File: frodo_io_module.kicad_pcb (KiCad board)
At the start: 4 copper layers, 58 x 58 mm, 198 parts, among them J1 Molex MicroFit 2x3, J10 Molex MicroFit 2x2, J11 Molex MicroFit 2x2, J12 JST-GH 4Pin, J13 JST-GH 4Pin, J2 Molex MicroFit 2x3, J3 SWD, J4 JST-GH 4Pin, J5 JST-GH 4Pin, J6 JST-GH 4Pin, J7 JST-GH 4Pin, J8 Molex MicroFit 2x2, J9 Molex MicroFit 2x2, Q1 NMOS, Q10 PMOS, Q11 PMOS, Q12 PMOS, Q13 PMOS, Q14 PMOS, Q15 PMOS, Q16 PMOS, Q17 NMOS, Q18 NMOS, Q2 NMOS, Q3 NMOS, Q4 NMOS, Q5 NMOS, Q6 NMOS, Q7 NMOS, Q8 NMOS, Q9 PMOS, SW1 SW_DIP_x06, U1 AZ1117H-ADJ, U10 STM32F103RCTx, U2 INA213, U3 AZ1117-3.3, U4 W25Q128JVP, U5 MCP2562-E-SN, U6 L7805, U7 L7805, U8 MCP4017-xxxxLT, U9 LM3488MM, Y1 8MHz 12pF

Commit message: add descriptors on silkscreen, add part numbers
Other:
- board text added: "5V"
- board text added: "BAT"
- board text added: "BST"
- board text added: "BUS A"
- board text added: "BUS B"
- board text added: "CHR"
- board text added: "COM0"
- board text added: "COM1"
- board text added: "COM2"
- board text added: "COM3"
- board text added: "COM4"
- board text added: "COM5"
- board text added: "OUT0"
- board text added: "OUT1"
- board text added: "OUT2"
- board text added: "OUT3"

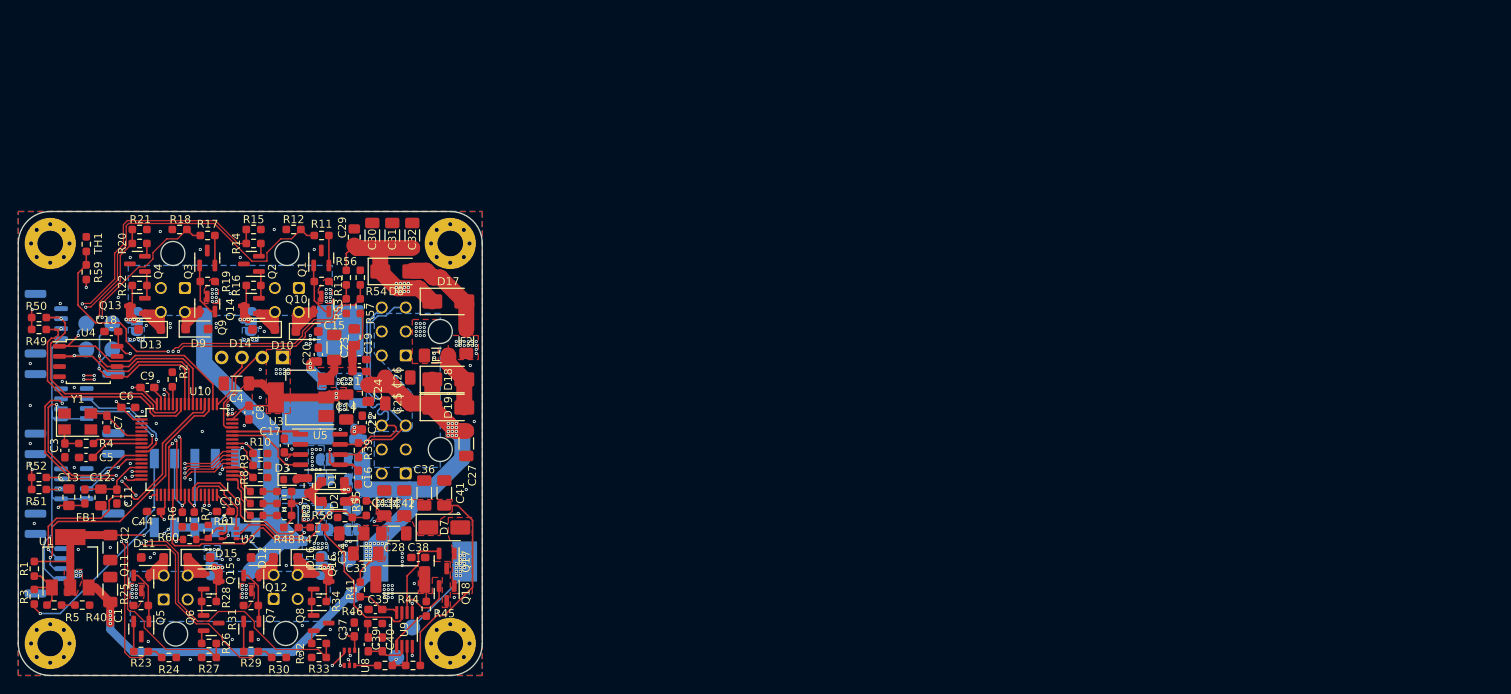
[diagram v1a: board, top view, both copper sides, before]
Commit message: updated scematic to new requirements
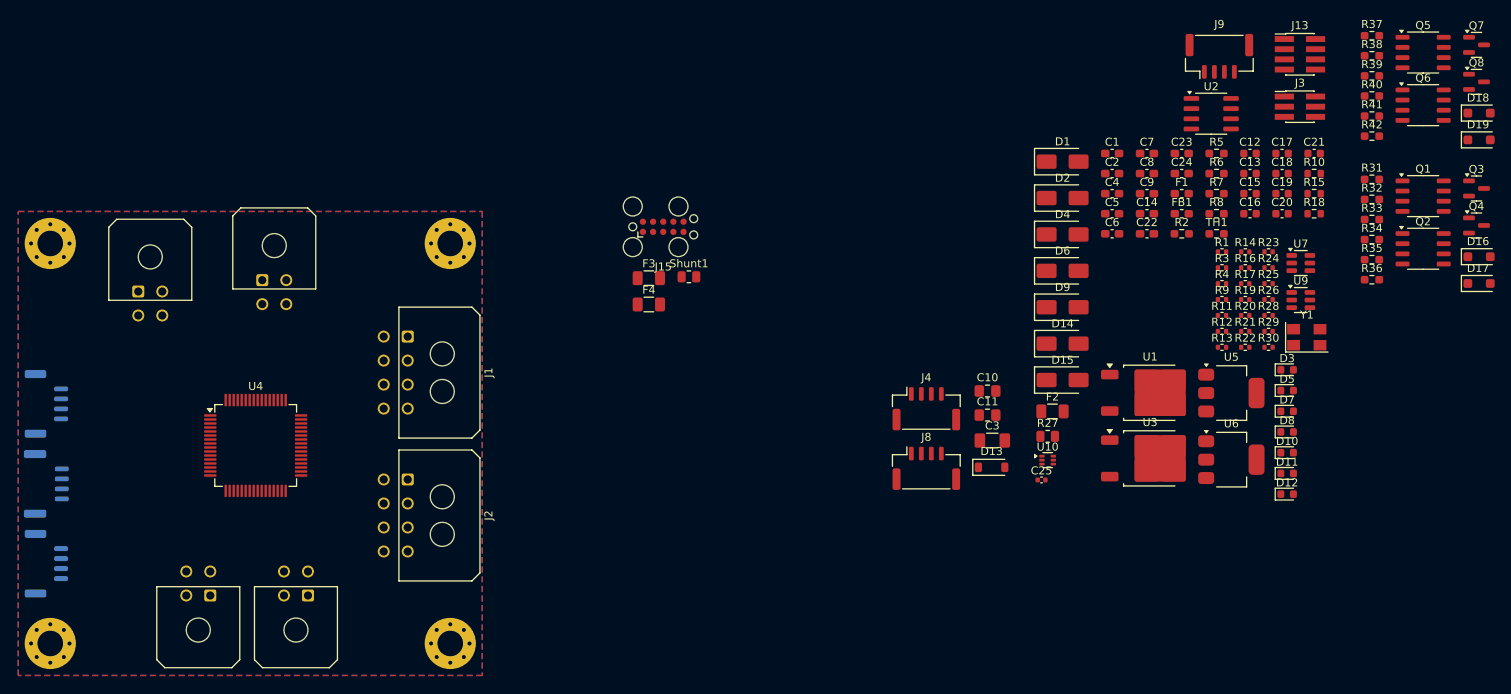
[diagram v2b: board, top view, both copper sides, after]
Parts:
- removed C26, C27, C28, C30, C31, C32, C33, C34: 22u, Capacitor_SMD:C_1206_3216Metric_Pad1.33x1.80mm_HandSolder
- removed C29: 1u, Capacitor_SMD:C_0805_2012Metric_Pad1.18x1.45mm_HandSolder
- removed C35, C37, C39, C44: 100n, Capacitor_SMD:C_0603_1608Metric_Pad1.08x0.95mm_HandSolder
- removed C36, C41, C42, C43: 10u, Capacitor_SMD:C_1206_3216Metric_Pad1.33x1.80mm_HandSolder
- removed C38: 10p, Capacitor_SMD:C_0603_1608Metric_Pad1.08x0.95mm_HandSolder
- removed C40: 3.3n, Capacitor_SMD:C_0603_1608Metric_Pad1.08x0.95mm_HandSolder
- removed G***: LOGO, frodo_io_module:rapid_logo
- removed JP1, JP2: +VSW_Sel, Jumper:SolderJumper-2_P1.3mm_Open_RoundedPad1.0x1.5mm
- removed JP10, JP11, JP12, JP9: servo_ss, Jumper:SolderJumper-3_P1.3mm_Open_RoundedPad1.0x1.5mm
- removed JP3, JP4: VDC_Sel, Jumper:SolderJumper-2_P1.3mm_Open_RoundedPad1.0x1.5mm
- removed JP5, JP6: Vext_Sel, Jumper:SolderJumper-2_P1.3mm_Open_RoundedPad1.0x1.5mm
- removed JP7, JP8: +5V_Sel, Jumper:SolderJumper-2_P1.3mm_Open_RoundedPad1.0x1.5mm
- removed L1: 15u, Inductor_SMD:L_Bourns_SRP1245A
- removed Q10, Q11, Q12, Q13, Q14, Q15, Q16, Q9: PMOS, Package_TO_SOT_SMD:SOT-23
- removed Q17, Q18: NMOS, Package_TO_SOT_SMD:SOT-23
- removed R43: 33k, Resistor_SMD:R_0603_1608Metric_Pad0.98x0.95mm_HandSolder
- removed R44: 10m, Resistor_SMD:R_2512_6332Metric_Pad1.40x3.35mm_HandSolder
- removed R45: 100, Resistor_SMD:R_0603_1608Metric_Pad0.98x0.95mm_HandSolder
- removed R46, R48: 1.5k, Resistor_SMD:R_0603_1608Metric_Pad0.98x0.95mm_HandSolder
- removed R47: 47k, Resistor_SMD:R_0603_1608Metric_Pad0.98x0.95mm_HandSolder
- removed R49, R50, R51, R52, R53: 4.7k, Resistor_SMD:R_0603_1608Metric_Pad0.98x0.95mm_HandSolder
- removed R54: 15k, Resistor_SMD:R_0603_1608Metric_Pad0.98x0.95mm_HandSolder
- removed R55: 22k, Resistor_SMD:R_0603_1608Metric_Pad0.98x0.95mm_HandSolder
- removed R56, R57, R58: 2.2k, Resistor_SMD:R_0603_1608Metric_Pad0.98x0.95mm_HandSolder
- removed R59: 10k, Resistor_SMD:R_0603_1608Metric_Pad0.98x0.95mm_HandSolder
- removed R60, R61: 10k, Resistor_SMD:R_0603_1608Metric
- removed R62: 5m, Resistor_SMD:R_2512_6332Metric
- removed SW1: SW_DIP_x06, Button_Switch_SMD:SW_DIP_SPSTx06_Slide_9.78x17.42mm_W8.61mm_P2.54mm
- removed TP1, TP10, TP2, TP3, TP4, TP7, TP8, TP9: TestPoint, TestPoint:TestPoint_Pad_D2.0mm
- removed U8: MCP4017-xxxxLT, Package_TO_SOT_SMD:SOT-363_SC-70-6
- added F3: 10A, Fuse:Fuse_1206_3216Metric, F.Cu at (178.8, 108.3)
- added F4: 10A, Fuse:Fuse_1206_3216Metric, F.Cu at (178.8, 111.6)
- added J14: ~, stigma:Molex_Micro-Fit_3.0_43045-0400_2x02_P3.00mm_Horizontal, F.Cu at (115.0, 110.0)
- added J15: TC2050, Connector:Tag-Connect_TC2050-IDC-FP_2x05_P1.27mm_Vertical, F.Cu at (180.6, 101.9)
- added Shunt1: 250mR 1%, Resistor_SMD:R_0805_2012Metric, F.Cu at (183.8, 108.2)
- C1, C4: value 10u -> 100n; footprint Capacitor_SMD:C_1206_3216Metric_Pad1.33x1.80mm_HandSolder -> Capacitor_SMD:C_0603_1608Metric_Pad1.08x0.95mm_HandSolder
- C10: value 100n -> 1u; footprint Capacitor_SMD:C_0603_1608Metric_Pad1.08x0.95mm_HandSolder -> Capacitor_SMD:C_0805_2012Metric_Pad1.18x1.45mm_HandSolder
- C11: value 22n -> 1u; footprint Capacitor_SMD:C_0603_1608Metric_Pad1.08x0.95mm_HandSolder -> Capacitor_SMD:C_0805_2012Metric_Pad1.18x1.45mm_HandSolder
- C12: value 1u -> 330n; footprint Capacitor_SMD:C_0805_2012Metric_Pad1.18x1.45mm_HandSolder -> Capacitor_SMD:C_0603_1608Metric
- C13: value 1u -> 100n; footprint Capacitor_SMD:C_0805_2012Metric_Pad1.18x1.45mm_HandSolder -> Capacitor_SMD:C_0603_1608Metric
- C14, C2: value 22u -> 100n; footprint Capacitor_SMD:C_1206_3216Metric_Pad1.33x1.80mm_HandSolder -> Capacitor_SMD:C_0603_1608Metric_Pad1.08x0.95mm_HandSolder
- C15: value 10u -> 330n; footprint Capacitor_SMD:C_1206_3216Metric_Pad1.33x1.80mm_HandSolder -> Capacitor_SMD:C_0603_1608Metric
- C16: footprint Capacitor_SMD:C_0603_1608Metric_Pad1.08x0.95mm_HandSolder -> Capacitor_SMD:C_0603_1608Metric
- C17, C20: value 100n -> 10u; footprint Capacitor_SMD:C_0603_1608Metric_Pad1.08x0.95mm_HandSolder -> Capacitor_SMD:C_0603_1608Metric
- C18: value 100n -> 22u; footprint Capacitor_SMD:C_0603_1608Metric_Pad1.08x0.95mm_HandSolder -> Capacitor_SMD:C_0603_1608Metric
- C19: value 330n -> 100n; footprint Capacitor_SMD:C_0603_1608Metric_Pad1.08x0.95mm_HandSolder -> Capacitor_SMD:C_0603_1608Metric
- C21: value 330n -> 22u; footprint Capacitor_SMD:C_0603_1608Metric_Pad1.08x0.95mm_HandSolder -> Capacitor_SMD:C_0603_1608Metric
- C22: value 100n -> 10p
- C23: value 1u -> 10p; footprint Capacitor_SMD:C_0805_2012Metric_Pad1.18x1.45mm_HandSolder -> Capacitor_SMD:C_0603_1608Metric_Pad1.08x0.95mm_HandSolder
- C24: value 1u -> 100n; footprint Capacitor_SMD:C_0805_2012Metric_Pad1.18x1.45mm_HandSolder -> Capacitor_SMD:C_0603_1608Metric_Pad1.08x0.95mm_HandSolder
- C25: value 22u -> 100n; footprint Capacitor_SMD:C_1206_3216Metric_Pad1.33x1.80mm_HandSolder -> Capacitor_SMD:C_0402_1005Metric
- C3: value 10p -> 10u; footprint Capacitor_SMD:C_0603_1608Metric_Pad1.08x0.95mm_HandSolder -> Capacitor_SMD:C_1206_3216Metric_Pad1.33x1.80mm_HandSolder
- C7: value 10p -> 100n
- C9: value 100n -> 22n
- D1: value D_Schottky -> D; footprint Diode_SMD:D_SOD-123F -> Diode_SMD:D_SMA
- D10, D12: value D -> LED; footprint Diode_SMD:D_SOD-123F -> LED_SMD:LED_0603_1608Metric
- D11: value D -> red; footprint Diode_SMD:D_SOD-123F -> LED_SMD:LED_0603_1608Metric
- D13: value D -> NRVB130T1G; footprint Diode_SMD:D_SOD-123F -> Diode_SMD:D_SOD-123
- D14, D15: footprint Diode_SMD:D_SOD-123F -> Diode_SMD:D_SMA
- D17, D18, D19: value D_Schottky -> D; footprint Diode_SMD:D_SMA -> Diode_SMD:D_SOD-123F
- D2: value D_Schottky -> SS34; footprint Diode_SMD:D_SOD-123F -> Diode_SMD:D_SMA
- D3, D5: value LED -> red
- D4, D6: value LED -> SS34; footprint LED_SMD:LED_0603_1608Metric -> Diode_SMD:D_SMA
- D7: value D_Schottky -> red; footprint Diode_SMD:D_SMA -> LED_SMD:LED_0603_1608Metric
- D8: value D_Schottky -> LED; footprint Diode_SMD:D_SMA -> LED_SMD:LED_0603_1608Metric
- D9: value D -> SS34; footprint Diode_SMD:D_SOD-123F -> Diode_SMD:D_SMA
- F1: value 10A -> 3A; footprint Fuse:Fuse_1206_3216Metric_Pad1.42x1.75mm_HandSolder -> Fuse:Fuse_0603_1608Metric_Pad1.05x0.95mm_HandSolder
- F2: footprint Fuse:Fuse_1206_3216Metric_Pad1.42x1.75mm_HandSolder -> Fuse:Fuse_1206_3216Metric
- J1, J2: value Molex MicroFit 2x3 -> Conn_02x04_Top_Bottom; footprint Connector_Molex:Molex_Micro-Fit_3.0_43045-0600_2x03_P3.00mm_Horizontal -> Connector_Molex:Molex_Micro-Fit_3.0_43045-0800_2x04_P3.00mm_Horizontal; moved to F.Cu
- J10, J11: value Molex MicroFit 2x2 -> ~; footprint Connector_Molex:Molex_Micro-Fit_3.0_43045-0400_2x02_P3.00mm_Horizontal -> stigma:Molex_Micro-Fit_3.0_43045-0400_2x02_P3.00mm_Horizontal; moved to F.Cu
- J12: value JST-GH 4Pin -> ~; footprint Connector_JST:JST_GH_BM04B-GHS-TBT_1x04-1MP_P1.25mm_Vertical -> stigma:Molex_Micro-Fit_3.0_43045-0400_2x02_P3.00mm_Horizontal; moved to F.Cu
- J13: value JST-GH 4Pin -> Conn_02x05_Counter_Clockwise; footprint Connector_JST:JST_GH_BM04B-GHS-TBT_1x04-1MP_P1.25mm_Vertical -> Connector_PinHeader_1.27mm:PinHeader_2x04_P1.27mm_Vertical_SMD; moved to F.Cu
- J3: value SWD -> Conn_02x03_Counter_Clockwise; footprint Connector_PinHeader_2.54mm:PinHeader_1x04_P2.54mm_Vertical -> Connector_PinHeader_1.27mm:PinHeader_2x03_P1.27mm_Vertical_SMD; moved to F.Cu
- J4: moved to F.Cu
- J6: footprint Connector_JST:JST_GH_SM04B-GHS-TB_1x04-1MP_P1.25mm_Horizontal -> Connector_JST:JST_GH_BM04B-GHS-TBT_1x04-1MP_P1.25mm_Vertical
- J8: value Molex MicroFit 2x2 -> JST-GH 4Pin; footprint Connector_Molex:Molex_Micro-Fit_3.0_43045-0400_2x02_P3.00mm_Horizontal -> Connector_JST:JST_GH_SM04B-GHS-TB_1x04-1MP_P1.25mm_Horizontal; moved to F.Cu
- J9: value Molex MicroFit 2x2 -> JST-GH 4Pin; footprint Connector_Molex:Molex_Micro-Fit_3.0_43045-0400_2x02_P3.00mm_Horizontal -> Connector_JST:JST_GH_BM04B-GHS-TBT_1x04-1MP_P1.25mm_Vertical; moved to F.Cu
- Q1, Q2, Q5, Q6: value NMOS -> AOSP21321; footprint Package_TO_SOT_SMD:SOT-23 -> Package_SO:SO-8_3.9x4.9mm_P1.27mm
- R1: value 680 -> 220; footprint Resistor_SMD:R_0603_1608Metric_Pad0.98x0.95mm_HandSolder -> Resistor_SMD:R_0402_1005Metric
- R10: value 10K -> 220; footprint Resistor_SMD:R_0603_1608Metric_Pad0.98x0.95mm_HandSolder -> Resistor_SMD:R_0603_1608Metric
- R11, R17: value 330 -> 310R; footprint Resistor_SMD:R_0603_1608Metric_Pad0.98x0.95mm_HandSolder -> Resistor_SMD:R_0402_1005Metric
- R12: value 10k -> 1k; footprint Resistor_SMD:R_0603_1608Metric_Pad0.98x0.95mm_HandSolder -> Resistor_SMD:R_0402_1005Metric
- R13, R16, R19, R4: value 1k -> 220; footprint Resistor_SMD:R_0603_1608Metric_Pad0.98x0.95mm_HandSolder -> Resistor_SMD:R_0402_1005Metric
- R14: value 330 -> 150R; footprint Resistor_SMD:R_0603_1608Metric_Pad0.98x0.95mm_HandSolder -> Resistor_SMD:R_0402_1005Metric
- R15: value 10k -> 220; footprint Resistor_SMD:R_0603_1608Metric_Pad0.98x0.95mm_HandSolder -> Resistor_SMD:R_0603_1608Metric
- R18: value 10k -> 60R; footprint Resistor_SMD:R_0603_1608Metric_Pad0.98x0.95mm_HandSolder -> Resistor_SMD:R_0603_1608Metric
- R2: value 10k -> 120, DNP
- R20: value 330 -> 22; footprint Resistor_SMD:R_0603_1608Metric_Pad0.98x0.95mm_HandSolder -> Resistor_SMD:R_0402_1005Metric
- R21: value 10k -> 22; footprint Resistor_SMD:R_0603_1608Metric_Pad0.98x0.95mm_HandSolder -> Resistor_SMD:R_0402_1005Metric
- R22: value 1k -> 22; footprint Resistor_SMD:R_0603_1608Metric_Pad0.98x0.95mm_HandSolder -> Resistor_SMD:R_0402_1005Metric
- R23, R26: value 330 -> 5k; footprint Resistor_SMD:R_0603_1608Metric_Pad0.98x0.95mm_HandSolder -> Resistor_SMD:R_0402_1005Metric
- R24: value 10k -> 5k; footprint Resistor_SMD:R_0603_1608Metric_Pad0.98x0.95mm_HandSolder -> Resistor_SMD:R_0402_1005Metric
- R25: value 1k -> 5k; footprint Resistor_SMD:R_0603_1608Metric_Pad0.98x0.95mm_HandSolder -> Resistor_SMD:R_0402_1005Metric
- R27: value 10k -> 10m; footprint Resistor_SMD:R_0603_1608Metric_Pad0.98x0.95mm_HandSolder -> Resistor_SMD:R_0805_2012Metric
- R28: value 1k -> 15k; footprint Resistor_SMD:R_0603_1608Metric_Pad0.98x0.95mm_HandSolder -> Resistor_SMD:R_0402_1005Metric
- R29: value 330 -> 15k; footprint Resistor_SMD:R_0603_1608Metric_Pad0.98x0.95mm_HandSolder -> Resistor_SMD:R_0402_1005Metric
- R3: value 820 -> 10k; footprint Resistor_SMD:R_0603_1608Metric_Pad0.98x0.95mm_HandSolder -> Resistor_SMD:R_0402_1005Metric
- R30: value 10k -> 15k; footprint Resistor_SMD:R_0603_1608Metric_Pad0.98x0.95mm_HandSolder -> Resistor_SMD:R_0402_1005Metric
- R32: value 330 -> 1k
- R33: value 10k -> 330
- R34: value 1k -> 330
- R35, R36: value 220 -> 10k
- R37: value 680 -> 1k
- R38: value 220 -> 1k
- R39: value 120, DNP -> 330
- R40: value 100 -> 330
- R41: value 22 -> 10k
- R42: value 1.5k -> 10k
- R5: value 1k -> 4.7k
- R6, R7, R8: value 10K -> 4.7k
- R9: value 10K -> 150R; footprint Resistor_SMD:R_0603_1608Metric_Pad0.98x0.95mm_HandSolder -> Resistor_SMD:R_0402_1005Metric
- U1: value AZ1117H-ADJ -> L7805; footprint Package_TO_SOT_SMD:SOT-223-3_TabPin2 -> Package_TO_SOT_SMD:TO-252-2
- U10: value STM32F103RCTx -> TPD4E1U06; footprint Package_QFP:LQFP-64_10x10mm_P0.5mm -> Package_TO_SOT_SMD:SOT-563
- U2: value INA213 -> MCP2562-E-SN; footprint Package_TO_SOT_SMD:SOT-363_SC-70-6 -> Package_SO:SOIC-8_3.9x4.9mm_P1.27mm
- U3: value AZ1117-3.3 -> L7805; footprint Package_TO_SOT_SMD:SOT-223-3_TabPin2 -> Package_TO_SOT_SMD:TO-252-2
- U4: value W25Q128JVP -> STM32F103RCTx; footprint Package_SO:SOIC-8_5.275x5.275mm_P1.27mm -> Package_QFP:LQFP-64_10x10mm_P0.5mm
- U5: value MCP2562-E-SN -> AZ1117H-ADJ; footprint Package_SO:SOIC-8_3.9x4.9mm_P1.27mm -> Package_TO_SOT_SMD:SOT-223-3_TabPin2
- U6: value L7805 -> AZ1117H-ADJ; footprint Package_TO_SOT_SMD:TO-252-2 -> Package_TO_SOT_SMD:SOT-223-3_TabPin2; moved to F.Cu
- U7: value L7805 -> INA181; footprint Package_TO_SOT_SMD:TO-252-2 -> Package_TO_SOT_SMD:SOT-23-6; moved to F.Cu
- U9: value LM3488MM -> INA181A2IDBVT; footprint Package_SO:MSOP-8_3x3mm_P0.65mm -> Package_TO_SOT_SMD:SOT-23-6
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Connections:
- C1 pad 1: +VSW_fused -> GND
- C1 pad 2: GND -> +3.3V
- C10 pad 1: +3.3V -> +3.3VA
- C11 pad 1: +3.3VA -> +3.3V
- C12 pad 1: +3.3VA -> GND
- C12 pad 2: GND -> main_voltage
- C13 pad 1: +3.3V -> GND
- C13 pad 2: GND -> Net-(D2-A)
- C14 pad 1: +3.3V -> NRST
- C15 pad 1: +VSW_fused -> GND
- C15 pad 2: GND -> main_voltage
- C16 pad 2: +3.3V -> Net-(D4-A)
- C18 pad 2: +3.3V -> Net-(D6-A)
- C19 pad 1: +VSW_fused -> +3.3V
- C2 pad 1: VSwitch -> GND
- C2 pad 2: GND -> +5V
- C20 pad 1: Net-(D1-A) -> GND
- C20 pad 2: GND -> +5V
- C21 pad 1: +VSW_fused -> GND
- C21 pad 2: GND -> Net-(D9-A)
- C22 pad 1: Net-(D2-A) -> Net-(C22-Pad1)
- C23 pad 1: +VSW_fused -> HSE_IN
- C24 pad 1: +VSW_fused -> GND
- C24 pad 2: GND -> +3.3V
- C25 pad 1: +VSW_fused -> GND
- C25 pad 2: GND -> +5V
- C3 pad 1: Net-(C3-Pad1) -> +3.3V
- C5 pad 1: /NRST -> +3.3V
- C7 pad 1: HSE_IN -> +3.3V
- C9 pad 1: +3.3V -> +3.3VA
- D1 pad 1: +5V -> Net-(D1-K)
- D10 pad 1: Net-(D10-K) -> STAT_LED1
- D10 pad 2: GND -> Net-(D10-A)
- D11 pad 1: Net-(D11-K) -> GND
- D11 pad 2: GND -> Net-(D11-A)
- D12 pad 1: Net-(D12-K) -> STAT_LED2
- D12 pad 2: GND -> Net-(D12-A)
- D13 pad 1: Net-(D13-K) -> /Digital Output/OUT1
- D13 pad 2: GND -> Net-(D13-A)
- D14 pad 1: Net-(D14-K) -> v_main_pre_sense
- D14 pad 2: GND -> high_current2
- D15 pad 1: Net-(D15-K) -> v_main_pre_sense
- D15 pad 2: GND -> high_current
- D16 pad 1: Net-(D16-K) -> /Digital Output/OUT1
- D17 pad 1: VDC_fused -> /Digital Output/OUT2
- D17 pad 2: Net-(D17-A) -> GND
- D18 pad 1: +VSW_fused -> /Digital Output1/OUT1
- D18 pad 2: Net-(D18-A) -> GND
- D19 pad 1: +VSW_fused -> /Digital Output1/OUT2
- D19 pad 2: Net-(D18-A) -> GND
- D4 pad 1: STAT_LED0 -> +5V
- D5 pad 1: STAT_LED1 -> GND
- D6 pad 1: STAT_LED2 -> +3.3V
- D7 pad 1: Vboost -> GND
- D7 pad 2: Vboost_FET_D -> Net-(D7-A)
- D8 pad 1: VDC_fused -> STAT_LED0
- D8 pad 2: Net-(D17-A) -> Net-(D8-A)
- D9 pad 1: Net-(D9-K) -> +3.3V
- D9 pad 2: GND -> Net-(D9-A)
- F1 pad 1: +VSW -> Net-(D1-K)
- F1 pad 2: Net-(D18-A) -> v_main_pre_sense
- F2 pad 1: VDC -> /Digital Output/VD
- F2 pad 2: Net-(D17-A) -> high_current
- J1 pad 3: CAN- -> CAN_1_L
- J1 pad 4: VDC -> CAN_2_L
- J1 pad 5: +VSW -> charging_voltage
- J1 pad 6: CAN+ -> Net-(D1-A)
- J10 pad 3: Net-(D11-K) -> high_current
- J10 pad 4: Net-(D15-K) -> high_current
- J11 pad 3: Net-(D12-K) -> /Digital Output/OUT2
- J11 pad 4: Net-(D16-K) -> /Digital Output/OUT1
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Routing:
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- removed copper zone on F.Cu, net +3.3V
- removed copper zone on In2.Cu, net +3.3V
- removed copper zone on B.Cu, net +5V
- removed copper zone on F.Cu, net +5V
- removed copper zone on B.Cu, net +VSW
- removed copper zone on F.Cu, net +VSW
- removed copper zone on B.Cu, net +VSW_fused
- removed copper zone on F.Cu, net +VSW_fused
- removed copper zone on F.Cu, net VDC
- removed copper zone on In2.Cu, net VDC
- removed copper zone on B.Cu, net VDC_fused
- removed copper zone on In2.Cu, net VDC_fused
- removed copper zone on B.Cu, net VSwitch
- removed copper zone on F.Cu, net VSwitch
- removed copper zone on B.Cu, net Vboost
- removed copper zone on F.Cu, net Vboost
- removed copper zone on F.Cu, net Vboost_FET_D
- removed copper zone on F.Cu, net Vboost_FET_S
- removed copper zone on B.Cu, net Vdrive
- removed copper zone on F.Cu, net Vdrive
- removed copper zone on B.Cu, net Vdrive_pre_I_sense
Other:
- board outline removed
- board text added: "RAPID IO Board"
- board text added: "rev 2"
- board text removed: "5V"
- board text removed: "BAT"
- board text removed: "BST"
- board text removed: "BUS A"
- board text removed: "BUS B"
- board text removed: "CHR"
- board text removed: "FRoDO IO Board"
- board text removed: "OUT0"
- board text removed: "OUT1"
- board text removed: "OUT2"
- board text removed: "OUT3"
- board text removed: "rev 1"

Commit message: some more changes to the io board
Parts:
- removed D17, D18, D19: D, Diode_SMD:D_SOD-123F
- removed J13: Conn_02x05_Counter_Clockwise, Connector_PinHeader_1.27mm:PinHeader_2x04_P1.27mm_Vertical_SMD
- removed R1: 220, Resistor_SMD:R_0402_1005Metric
- removed R3: 10k, Resistor_SMD:R_0402_1005Metric
- added C26: 100n, Capacitor_SMD:C_0402_1005Metric, F.Cu at (126.0, 29.2)
- added C27: 100n, Capacitor_SMD:C_0402_1005Metric, F.Cu at (-215.1, 156.2)
- added C28: 100n, Capacitor_SMD:C_0402_1005Metric, F.Cu at (-195.0, 164.6)
- added C29: 100n, Capacitor_SMD:C_0402_1005Metric, F.Cu at (57.1, 30.8)
- added C30: 100n, Capacitor_SMD:C_0402_1005Metric, F.Cu at (57.1, 32.8)
- added D21: D, Diode_SMD:D_SOD-323_HandSoldering, F.Cu at (86.5, 151.3)
- added D22: D, Diode_SMD:D_SOD-323_HandSoldering, F.Cu at (79.5, 151.3)
- added D23: D, Diode_SMD:D_SOD-323_HandSoldering, F.Cu at (86.5, 154.3)
- added D24: D, Diode_SMD:D_SOD-323_HandSoldering, F.Cu at (79.5, 154.3)
- added J16: TC2050, Connector:Tag-Connect_TC2050-IDC-FP_2x05_P1.27mm_Vertical, F.Cu at (-72.1, 188.1)
- added R43: 330, Resistor_SMD:R_0603_1608Metric_Pad0.98x0.95mm_HandSolder, F.Cu at (190.0, 238.7)
- added R44: 10k, Resistor_SMD:R_0603_1608Metric_Pad0.98x0.95mm_HandSolder, F.Cu at (190.0, 241.2)
- added R45: 10k, Resistor_SMD:R_0603_1608Metric_Pad0.98x0.95mm_HandSolder, F.Cu at (190.0, 243.7)
- added R46: 1k, Resistor_SMD:R_0603_1608Metric_Pad0.98x0.95mm_HandSolder, F.Cu at (-87.8, 184.6)
- added R47: 1k, Resistor_SMD:R_0603_1608Metric_Pad0.98x0.95mm_HandSolder, F.Cu at (-87.8, 187.1)
- added R48: 330, Resistor_SMD:R_0603_1608Metric_Pad0.98x0.95mm_HandSolder, F.Cu at (-87.8, 189.6)
- added R49: 330, Resistor_SMD:R_0603_1608Metric_Pad0.98x0.95mm_HandSolder, F.Cu at (-87.8, 192.1)
- added R50: 10k, Resistor_SMD:R_0603_1608Metric_Pad0.98x0.95mm_HandSolder, F.Cu at (-87.8, 194.7)
- added R51: 10k, Resistor_SMD:R_0603_1608Metric_Pad0.98x0.95mm_HandSolder, F.Cu at (-87.8, 197.2)
- added R52: 300, Resistor_SMD:R_0402_1005Metric, F.Cu at (320.7, 176.3)
- added R53: 220, Resistor_SMD:R_0402_1005Metric, F.Cu at (320.7, 178.3)
- added SW1: KMR721NGLFS, Button_Switch_SMD:SW_Push_1P1T_NO_CK_KMR2, F.Cu at (182.4, 65.8)
- added SW2: KMR721NGLFS, Button_Switch_SMD:SW_Push_1P1T_NO_CK_KMR2, F.Cu at (182.4, 70.4)
- added SW3: KMR721NGLFS, Button_Switch_SMD:SW_Push_1P1T_NO_CK_KMR2, F.Cu at (-74.8, 195.2)
- added U11: MCP2562-E-SN, Package_SO:SOIC-8_3.9x4.9mm_P1.27mm, F.Cu at (38.6, 91.7)
- added U12: TPD4E1U06, Package_TO_SOT_SMD:SOT-563, F.Cu at (-69.3, 194.4)
- added U8: MCP2562-E-SN, Package_SO:SOIC-8_3.9x4.9mm_P1.27mm, F.Cu at (-209.7, 117.6)
- C1: value 100n -> 4.7u; footprint Capacitor_SMD:C_0603_1608Metric_Pad1.08x0.95mm_HandSolder -> Capacitor_SMD:C_0402_1005Metric
- C10: value 1u -> 10n; footprint Capacitor_SMD:C_0805_2012Metric_Pad1.18x1.45mm_HandSolder -> Capacitor_SMD:C_0402_1005Metric
- C11: value 1u -> 330n; footprint Capacitor_SMD:C_0805_2012Metric_Pad1.18x1.45mm_HandSolder -> Capacitor_SMD:C_0603_1608Metric
- C12, C15: value 330n -> 100n; footprint Capacitor_SMD:C_0603_1608Metric -> Capacitor_SMD:C_0402_1005Metric
- C13: value 100n -> 330n
- C14, C2, C24, C4, C5, C6: footprint Capacitor_SMD:C_0603_1608Metric_Pad1.08x0.95mm_HandSolder -> Capacitor_SMD:C_0402_1005Metric
- C16: value 100n -> 10u; footprint Capacitor_SMD:C_0603_1608Metric -> Capacitor_SMD:C_0402_1005Metric
- C17: value 10u -> 22u; footprint Capacitor_SMD:C_0603_1608Metric -> Capacitor_SMD:C_0402_1005Metric
- C18: value 22u -> 10p; footprint Capacitor_SMD:C_0603_1608Metric -> Capacitor_SMD:C_0402_1005Metric
- C19: value 100n -> 10p; footprint Capacitor_SMD:C_0603_1608Metric -> Capacitor_SMD:C_0402_1005Metric
- C20: value 10u -> 100n; footprint Capacitor_SMD:C_0603_1608Metric -> Capacitor_SMD:C_0402_1005Metric
- C21: value 22u -> 10u; footprint Capacitor_SMD:C_0603_1608Metric -> Capacitor_SMD:C_0402_1005Metric
- C22: value 10p -> 22u; footprint Capacitor_SMD:C_0603_1608Metric_Pad1.08x0.95mm_HandSolder -> Capacitor_SMD:C_0402_1005Metric
- C23: value 10p -> 100n; footprint Capacitor_SMD:C_0603_1608Metric_Pad1.08x0.95mm_HandSolder -> Capacitor_SMD:C_0402_1005Metric
- C3: value 10u -> 100n; footprint Capacitor_SMD:C_1206_3216Metric_Pad1.33x1.80mm_HandSolder -> Capacitor_SMD:C_0402_1005Metric
- C7: value 100n -> 10n; footprint Capacitor_SMD:C_0603_1608Metric_Pad1.08x0.95mm_HandSolder -> Capacitor_SMD:C_0402_1005Metric
- C8: value 100n -> 1u; footprint Capacitor_SMD:C_0603_1608Metric_Pad1.08x0.95mm_HandSolder -> Capacitor_SMD:C_0402_1005Metric
- C9: value 22n -> 1u; footprint Capacitor_SMD:C_0603_1608Metric_Pad1.08x0.95mm_HandSolder -> Capacitor_SMD:C_0402_1005Metric
- D10: value LED -> yellow
- D12: value LED -> green
- D14: value D -> ~; footprint Diode_SMD:D_SMA -> Diode_SMD:D_SOD-123
- D15: footprint Diode_SMD:D_SMA -> Diode_SMD:D_SOD-123F
- D2, D4, D6: value SS34 -> RB070MM-30TR; footprint Diode_SMD:D_SMA -> Diode_SMD:D_SOD-123F
- D8: value LED -> RB070MM-30TR; footprint LED_SMD:LED_0603_1608Metric -> Diode_SMD:D_SOD-123F
- D9: value SS34 -> red; footprint Diode_SMD:D_SMA -> LED_SMD:LED_0603_1608Metric
- FB1: footprint Inductor_SMD:L_0603_1608Metric_Pad1.05x0.95mm_HandSolder -> Inductor_SMD:L_0603_1608Metric
- J1, J11, J12, J8: moved to B.Cu
- J10: value ~ -> JST-GH 4Pin; footprint stigma:Molex_Micro-Fit_3.0_43045-0400_2x02_P3.00mm_Horizontal -> Connector_JST:JST_GH_BM04B-GHS-TBT_1x04-1MP_P1.25mm_Vertical; moved to B.Cu
- J14: value ~ -> USB_C_Receptacle_USB2.0; footprint stigma:Molex_Micro-Fit_3.0_43045-0400_2x02_P3.00mm_Horizontal -> Connector_USB:USB_C_Receptacle_Palconn_UTC16-G; moved to B.Cu
- J15: value TC2050 -> ~; footprint Connector:Tag-Connect_TC2050-IDC-FP_2x05_P1.27mm_Vertical -> stigma:Molex_Micro-Fit_3.0_43045-0400_2x02_P3.00mm_Horizontal; moved to B.Cu
- J2: value Conn_02x04_Top_Bottom -> Conn_02x05_Counter_Clockwise; footprint Connector_Molex:Molex_Micro-Fit_3.0_43045-0800_2x04_P3.00mm_Horizontal -> Connector_PinHeader_1.27mm:PinHeader_2x04_P1.27mm_Vertical_SMD; moved to B.Cu
- J3: value Conn_02x03_Counter_Clockwise -> Conn_02x04_Top_Bottom; footprint Connector_PinHeader_1.27mm:PinHeader_2x03_P1.27mm_Vertical_SMD -> Connector_Molex:Molex_Micro-Fit_3.0_43045-0800_2x04_P3.00mm_Horizontal; moved to B.Cu
- J4: value JST-GH 4Pin -> Conn_02x03_Counter_Clockwise; footprint Connector_JST:JST_GH_SM04B-GHS-TB_1x04-1MP_P1.25mm_Horizontal -> Connector_PinHeader_1.27mm:PinHeader_2x03_P1.27mm_Vertical_SMD; moved to B.Cu
- J6: footprint Connector_JST:JST_GH_BM04B-GHS-TBT_1x04-1MP_P1.25mm_Vertical -> Connector_JST:JST_GH_SM04B-GHS-TB_1x04-1MP_P1.25mm_Horizontal
- J7: footprint Connector_JST:JST_GH_SM04B-GHS-TB_1x04-1MP_P1.25mm_Horizontal -> Connector_JST:JST_GH_BM04B-GHS-TBT_1x04-1MP_P1.25mm_Vertical
- J9: footprint Connector_JST:JST_GH_BM04B-GHS-TBT_1x04-1MP_P1.25mm_Vertical -> Connector_JST:JST_GH_SM04B-GHS-TB_1x04-1MP_P1.25mm_Horizontal; moved to B.Cu
- R10, R15: footprint Resistor_SMD:R_0603_1608Metric -> Resistor_SMD:R_0402_1005Metric
- R11: value 310R -> 150R
- R14: value 150R -> 1k
- R16: value 220 -> 60R; footprint Resistor_SMD:R_0402_1005Metric -> Resistor_SMD:R_0603_1608Metric
- R17: value 310R -> 300
- R18: value 60R -> 1k; footprint Resistor_SMD:R_0603_1608Metric -> Resistor_SMD:R_0402_1005Metric
- R19: value 220 -> 1k
- R2: value 120, DNP -> 1k; footprint Resistor_SMD:R_0603_1608Metric_Pad0.98x0.95mm_HandSolder -> Resistor_SMD:R_0402_1005Metric
- R20: value 22 -> 100k
- R21: value 22 -> 4k7
- R22: value 22 -> 5k1
- R23: value 5k -> 5k1
- R24: value 5k -> 10k
- R25, R26: value 5k -> 22R
- R27: value 10m -> 120, DNP; footprint Resistor_SMD:R_0805_2012Metric -> Resistor_SMD:R_0603_1608Metric_Pad0.98x0.95mm_HandSolder
- R28, R29, R30: value 15k -> 22
- R31, R32: value 1k -> 5k; footprint Resistor_SMD:R_0603_1608Metric_Pad0.98x0.95mm_HandSolder -> Resistor_SMD:R_0402_1005Metric
- R33, R34: value 330 -> 5k; footprint Resistor_SMD:R_0603_1608Metric_Pad0.98x0.95mm_HandSolder -> Resistor_SMD:R_0402_1005Metric
- R35: value 10k -> 10m; footprint Resistor_SMD:R_0603_1608Metric_Pad0.98x0.95mm_HandSolder -> Resistor_SMD:R_0805_2012Metric
- R36: value 10k -> 120, DNP
- R37, R38: value 1k -> 15k; footprint Resistor_SMD:R_0603_1608Metric_Pad0.98x0.95mm_HandSolder -> Resistor_SMD:R_0402_1005Metric
- R39: value 330 -> 15k; footprint Resistor_SMD:R_0603_1608Metric_Pad0.98x0.95mm_HandSolder -> Resistor_SMD:R_0402_1005Metric
- R4: value 220 -> 100k
- R40: value 330 -> 1k
- R41: value 10k -> 1k
- R42: value 10k -> 330
- U10: value TPD4E1U06 -> INA181A2IDBVT; footprint Package_TO_SOT_SMD:SOT-563 -> Package_TO_SOT_SMD:SOT-23-6
- U2: value MCP2562-E-SN -> L7805; footprint Package_SO:SOIC-8_3.9x4.9mm_P1.27mm -> Package_TO_SOT_SMD:TO-252-2
- U3: value L7805 -> STM32F105RCTx; footprint Package_TO_SOT_SMD:TO-252-2 -> Package_QFP:LQFP-64_10x10mm_P0.5mm
- U4: value STM32F103RCTx -> AZ1117H-ADJ; footprint Package_QFP:LQFP-64_10x10mm_P0.5mm -> Package_TO_SOT_SMD:SOT-223-3_TabPin2
- U6: value AZ1117H-ADJ -> INA181; footprint Package_TO_SOT_SMD:SOT-223-3_TabPin2 -> Package_TO_SOT_SMD:SOT-23-6
- U9: value INA181A2IDBVT -> TPD4E1U06; footprint Package_TO_SOT_SMD:SOT-23-6 -> Package_TO_SOT_SMD:SOT-563
- moved R30 449.7 mm to (-191.6, 157.3)
- moved C24 443.7 mm to (-197.9, 113.0)
- moved R20 441.3 mm to (-188.0, 115.0)
- moved U10 436.1 mm to (-206.7, 156.1)
- moved C25 425.8 mm to (-197.7, 119.5)
- moved Y1 356.0 mm to (-89.8, 55.2), turned to 90 degrees
- moved C21 351.2 mm to (-87.3, 56.4), turned to 90 degrees
- moved R11 340.9 mm to (-85.7, 56.3), turned to 180 degrees
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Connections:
- C1 pad 1: GND -> +3.3V
- C1 pad 2: +3.3V -> GND
- C10 pad 1: +3.3VA -> +3.3V
- C11 pad 1: +3.3V -> GND
- C11 pad 2: GND -> main_voltage
- C12 pad 2: main_voltage -> Net-(D2-A)
- C13 pad 2: Net-(D2-A) -> main_voltage
- C14 pad 1: NRST -> GND
- C14 pad 2: GND -> Net-(D4-A)
- C15 pad 2: main_voltage -> NRST
- C16 pad 2: Net-(D4-A) -> +5V
- C17 pad 2: +5V -> Net-(D6-A)
- C18 pad 1: GND -> Net-(C18-Pad1)
- C18 pad 2: Net-(D6-A) -> GND
- C19 pad 1: +3.3V -> HSE_IN
- C2 pad 1: GND -> +3.3V
- C2 pad 2: +5V -> GND
- C20 pad 1: GND -> +3.3V
- C20 pad 2: +5V -> GND
- C21 pad 2: Net-(D9-A) -> +5V
- C22 pad 1: Net-(C22-Pad1) -> GND
- C22 pad 2: GND -> Net-(D8-A)
- C23 pad 1: HSE_IN -> GND
- C23 pad 2: GND -> +3.3V
- C24 pad 2: +3.3V -> /VBUS
- C25 pad 2: +5V -> +3.3V
- C7 pad 1: +3.3V -> +3.3VA
- C8 pad 1: +3.3V -> +3.3VA
- C9 pad 1: +3.3VA -> +3.3V
- D13 pad 1: /Digital Output/OUT1 -> /Digital Output/OUT2
- D14 pad 1: v_main_pre_sense -> +5V
- D14 pad 2: high_current2 -> /VBUS
- D15 pad 2: high_current -> high_current2
- D16 pad 1: /Digital Output/OUT1 -> v_main_pre_sense
- D16 pad 2: GND -> high_current
- D8 pad 1: STAT_LED0 -> +3.3V
- D9 pad 1: +3.3V -> STAT_LED0
- J10 pad 1: GND -> +3.3V
- J10 pad 2: GND -> AIN2
- J10 pad 3: high_current -> AIN3
- J10 pad 4: high_current -> GND
- J11 pad 3: /Digital Output/OUT2 -> high_current
- J11 pad 4: /Digital Output/OUT1 -> high_current2
- J12 pad 3: high_current2 -> /Digital Output/OUT2
- J12 pad 4: high_current2 -> /Digital Output/OUT1
- J15 pad 1: NRST -> /Digital Output1/OUT1
- J15 pad 2: /J1-SWDIO -> /Digital Output1/OUT2
- J2 pad 1: GND -> unconnected-(J2-Pin_1-Pad1)
- J2 pad 2: GND -> unconnected-(J2-Pin_2-Pad2)
- J2 pad 3: CAN_1_L -> unconnected-(J2-Pin_3-Pad3)
- J2 pad 4: CAN_2_L -> unconnected-(J2-Pin_4-Pad4)
- J2 pad 5: charging_voltage -> unconnected-(J2-Pin_5-Pad5)
- J2 pad 6: Net-(D1-A) -> unconnected-(J2-Pin_6-Pad6)
- J2 pad 7: CAN_1_H -> unconnected-(J2-Pin_7-Pad7)
- J2 pad 8: CAN_2_H -> unconnected-(J2-Pin_8-Pad8)
- J3 pad 1: +3.3V -> GND
- J3 pad 2: VS1 -> GND
- J3 pad 3: +5V -> CAN_1_L
- J3 pad 4: +5V -> CAN_2_L
- J3 pad 5: VS2 -> charging_voltage
- J3 pad 6: +3.3V -> Net-(D1-A)
- J4 pad 1: VS1 -> +3.3V
- J4 pad 2: U1_TX-I2C1_SCL -> VS1
- J4 pad 3: U1_RX-I2C1_SDA -> +5V
- J4 pad 4: GND -> +5V
- J5 pad 1: +3.3V -> VS1
- J5 pad 2: U2_TX-AIN4 -> U1_TX-I2C1_SCL
- J5 pad 3: U2_RX-AIN5 -> U1_RX-I2C1_SDA
- J6 pad 2: AIN0 -> U2_TX-AIN4
- J6 pad 3: AIN1 -> U2_RX-AIN5
- J7 pad 1: VS2 -> +3.3V
- J7 pad 2: U3_TX-I2C2_SCL -> AIN0
- J7 pad 3: U3_RX-I2C2_SDA -> AIN1
- J8 pad 1: +3.3V -> VS2
- J8 pad 2: U4_TX -> U3_TX-I2C2_SCL
- J8 pad 3: U4_RX -> U3_RX-I2C2_SDA
- J9 pad 2: AIN2 -> U4_TX
- J9 pad 3: AIN3 -> U4_RX
- R11 pad 1: Net-(U5-GND) -> Net-(D8-A)
- R11 pad 2: GND -> Net-(U5-GND)
- R12 pad 2: Net-(C22-Pad1) -> Net-(C18-Pad1)
- R13 pad 1: +3.3V -> Net-(D8-A)
- R13 pad 2: Net-(D8-A) -> Net-(D11-A)
- R14 pad 1: Net-(D9-A) -> +3.3V
- R14 pad 2: Net-(U6-GND) -> Net-(D9-A)
- R15 pad 1: Net-(D9-A) -> Net-(D2-A)
- R15 pad 2: Net-(D11-A) -> Net-(D3-A)
- R16 pad 1: +3.3V -> cont_check
- R16 pad 2: Net-(D10-A) -> Net-(U6-+)
- R17 pad 1: Net-(U6-GND) -> Net-(U5-GND)
- R18 pad 1: cont_check -> +3.3V
- R18 pad 2: Net-(U7-+) -> Net-(D10-A)
- R2 pad 1: CAN_1_H -> Net-(SW1-B)
- R2 pad 2: CAN_1_L -> +3.3V
- R20 pad 1: SWDIO -> GND
- R20 pad 2: /J1-SWDIO -> SWITCH
- R21 pad 1: SWO -> USB_FS_VBUS
- R21 pad 2: /J1-SWO -> /VBUS
- R22 pad 1: Net-(J15-Pin_6) -> Net-(J14-CC1)
- R22 pad 2: SWCLK -> GND
- R23 pad 1: v_main_pre_sense -> Net-(J14-CC2)
- R23 pad 2: vmain_sense -> GND
- R24 pad 1: high_current -> GND
- R24 pad 2: hc_sense -> USB_FS_VBUS
- R25 pad 1: high_current2 -> /D0-
- R25 pad 2: hc2_sense -> USB_D-
- R26 pad 1: +5V -> USB_D+
- R26 pad 2: TH_sense -> /D0+
- R27 pad 1: v_main_pre_sense -> CAN_1_H
- R27 pad 2: main_voltage -> CAN_1_L
- R28 pad 1: vmain_sense -> SWDIO
- R28 pad 2: GND -> /J1-SWDIO
- R29 pad 1: hc_sense -> SWO
- R29 pad 2: GND -> /J1-SWO
- R30 pad 1: hc2_sense -> Net-(J16-Pin_6)
- R30 pad 2: GND -> SWCLK
- R31 pad 1: /Digital Output/VD -> v_main_pre_sense
- R31 pad 2: Net-(Q1-G) -> vmain_sense
- R32 pad 1: /Digital Output/VD -> high_current
- R32 pad 2: Net-(Q2-G) -> hc_sense
- R33 pad 1: S1O1 -> high_current2
- R33 pad 2: Net-(Q3-G) -> hc2_sense
- R34 pad 1: S1O2 -> +5V
- R34 pad 2: Net-(Q4-G) -> TH_sense
- R35 pad 1: S1O1 -> v_main_pre_sense
- R35 pad 2: GND -> main_voltage
- R36 pad 1: S1O2 -> CAN_2_H
- R36 pad 2: GND -> CAN_2_L
- R37 pad 1: /Digital Output1/VD -> vmain_sense
- R37 pad 2: Net-(Q5-G) -> GND
- R38 pad 1: /Digital Output1/VD -> hc_sense
- R38 pad 2: Net-(Q6-G) -> GND
- R39 pad 1: S2O1 -> hc2_sense
- R39 pad 2: Net-(Q7-G) -> GND
- R4 pad 1: Net-(D4-A) -> GND
- R4 pad 2: Net-(D5-A) -> BOOT
- R40 pad 1: S2O2 -> /Digital Output/VD
- R40 pad 2: Net-(Q8-G) -> Net-(Q1-G)
- R41 pad 1: S2O1 -> /Digital Output/VD
- R41 pad 2: GND -> Net-(Q2-G)
- R42 pad 1: S2O2 -> S1O1
- R42 pad 2: GND -> Net-(Q3-G)
- R9 pad 2: Net-(U5-GND) -> Net-(U4-GND)
- Shunt1 pad 1: Net-(U7-+) -> Net-(U6-+)
- U10 pad 1: /J1-SWO -> I_sense
- U10 pad 2: /J1-SWDIO -> GND
- U10 pad 3: GND -> v_main_pre_sense
- U10 pad 4: Net-(J15-Pin_6) -> main_voltage
- U10 pad 5: +3.3V -> GND
- U10 pad 6: +5V -> +3.3V
- U2 pad 1: CAN_TX -> main_voltage
- U2 pad 3: +5V -> Net-(D4-A)
- U3 pad 1: main_voltage -> +3.3V
- U3 pad 2: GND -> unconnected-(U3-PC13-Pad2)
- U3 pad 3: Net-(D4-A) -> unconnected-(U3-PC14-Pad3)
- U4 pad 1: +3.3V -> Net-(U4-GND)
- U4 pad 2: unconnected-(U4-PC13-Pad2) -> Net-(D6-A)
- U4 pad 3: unconnected-(U4-PC14-Pad3) -> +5V
- U5 pad 2: Net-(D6-A) -> Net-(D8-A)
- U6 pad 1: Net-(U6-GND) -> adc_cont_check
- U6 pad 2: Net-(D9-A) -> GND
- U6 pad 3: +5V -> Net-(U6-+)
- U9 pad 1: I_sense -> BOOT
- U9 pad 2: GND -> NRST
- U9 pad 3: v_main_pre_sense -> GND
- U9 pad 4: main_voltage -> /D0+
- U9 pad 5: GND -> /D0-
- U9 pad 6: +3.3V -> /VBUS
- Y1 pad 1: Net-(C22-Pad1) -> Net-(C18-Pad1)
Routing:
- net +3.3V: track 0.00 -> 15.4 mm
- net GND: track 0.00 -> 11.9 mm
- net HSE_IN: track 0.00 -> 10.7 mm
- net HSE_OUT: track 0.00 -> 4.36 mm
- net +3.3VA: track 0.00 -> 3.73 mm
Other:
- board outline added: 55 x 55 mm
- board text removed: "COM0"

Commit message: Organize Components into groups.
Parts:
- moved U10 429.1 mm to (220.2, 113.0)
- moved U8 412.7 mm to (202.8, 130.8)
- moved C12 356.2 mm to (28.7, 21.9)
- moved C15 352.4 mm to (28.3, 35.5)
- moved J16 331.5 mm to (234.5, 62.2)
- moved SW3 319.4 mm to (201.4, 34.9)
- moved R30 316.2 mm to (106.2, 51.2)
- moved D10 315.2 mm to (257.1, 22.8)
- moved D12 314.9 mm to (257.4, 34.2)
- moved C17 313.8 mm to (28.5, 43.4)
- moved C16 313.7 mm to (28.2, 39.7)
- moved C19 313.2 mm to (28.1, 51.9)
- moved C20 313.2 mm to (28.1, 54.4)
- moved D13 306.8 mm to (265.2, 18.5)
- moved D8 305.0 mm to (247.9, 34.7)
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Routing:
- net Net-(D8-A): track 0.00 -> 4.36 mm
- net HSE_OUT: track 4.36 -> 0.00 mm
- net +3.3V: track 15.4 -> 16.8 mm
- net GND: track 11.9 -> 12.9 mm

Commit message: some more pin assignments
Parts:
- added FB10: BLM15PD121SN1D, Inductor_SMD:L_0402_1005Metric, F.Cu at (174.6, 74.0)
- added FB11: BLM15PD121SN1D, Inductor_SMD:L_0402_1005Metric, F.Cu at (177.5, 68.0)
- added FB12: BLM15PD121SN1D, Inductor_SMD:L_0402_1005Metric, F.Cu at (177.5, 70.0)
- added FB13: BLM15PD121SN1D, Inductor_SMD:L_0402_1005Metric, F.Cu at (177.5, 72.0)
- added FB14: BLM15PD121SN1D, Inductor_SMD:L_0402_1005Metric, F.Cu at (177.5, 74.0)
- added FB3: BLM15PD121SN1D, Inductor_SMD:L_0402_1005Metric, F.Cu at (171.6, 68.0)
- added FB4: BLM15PD121SN1D, Inductor_SMD:L_0402_1005Metric, F.Cu at (171.6, 70.0)
- added FB5: BLM15PD121SN1D, Inductor_SMD:L_0402_1005Metric, F.Cu at (171.6, 72.0)
- added FB6: BLM15PD121SN1D, Inductor_SMD:L_0402_1005Metric, F.Cu at (171.6, 74.0)
- added FB7: BLM15PD121SN1D, Inductor_SMD:L_0402_1005Metric, F.Cu at (174.6, 68.0)
- added FB8: BLM15PD121SN1D, Inductor_SMD:L_0402_1005Metric, F.Cu at (174.6, 70.0)
- added FB9: BLM15PD121SN1D, Inductor_SMD:L_0402_1005Metric, F.Cu at (174.6, 72.0)
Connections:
- J10 pad 2: AIN2 -> Net-(J10-Pin_2)
- J10 pad 3: AIN3 -> Net-(J10-Pin_3)
- J5 pad 2: U1_TX-I2C1_SCL -> Net-(J5-Pin_2)
- J5 pad 3: U1_RX-I2C1_SDA -> Net-(J5-Pin_3)
- J6 pad 2: U2_TX-AIN4 -> Net-(J6-Pin_2)
- J6 pad 3: U2_RX-AIN5 -> Net-(J6-Pin_3)
- J7 pad 2: AIN0 -> Net-(J7-Pin_2)
- J7 pad 3: AIN1 -> Net-(J7-Pin_3)
- J8 pad 2: U3_TX-I2C2_SCL -> Net-(J8-Pin_2)
- J8 pad 3: U3_RX-I2C2_SDA -> Net-(J8-Pin_3)
- J9 pad 2: U4_TX -> Net-(J9-Pin_2)
- J9 pad 3: U4_RX -> Net-(J9-Pin_3)
- R42 pad 1: S1O1 -> HC_OUT_1
- R43 pad 1: S1O2 -> HC_OUT_2
- R44 pad 1: S1O1 -> HC_OUT_1
- R45 pad 1: S1O2 -> HC_OUT_2
- R48 pad 1: S2O1 -> HC_OUT_3
- R49 pad 1: S2O2 -> HC_OUT_4
- R50 pad 1: S2O1 -> HC_OUT_3
- R51 pad 1: S2O2 -> HC_OUT_4
- U10 pad 1: I_sense -> I_sense_main
- U3 pad 10: unconnected-(U3-PC2-Pad10) -> hc_sense
- U3 pad 11: unconnected-(U3-PC3-Pad11) -> hc2_sense
- U3 pad 14: unconnected-(U3-PA0-Pad14) -> AIN0
- U3 pad 15: unconnected-(U3-PA1-Pad15) -> AIN1
- U3 pad 16: unconnected-(U3-PA2-Pad16) -> COM3_1
- U3 pad 17: unconnected-(U3-PA3-Pad17) -> COM3_2
- U3 pad 20: unconnected-(U3-PA4-Pad20) -> TH_sense
- U3 pad 21: SPI1_SCK -> unconnected-(U3-PA5-Pad21)
- U3 pad 22: SPI1_MISO -> unconnected-(U3-PA6-Pad22)
- U3 pad 23: SPI1_MOSI -> unconnected-(U3-PA7-Pad23)
- U3 pad 24: unconnected-(U3-PC4-Pad24) -> AIN2
- U3 pad 25: unconnected-(U3-PC5-Pad25) -> AIN3
- U3 pad 26: unconnected-(U3-PB0-Pad26) -> HC_OUT_3
- U3 pad 27: unconnected-(U3-PB1-Pad27) -> HC_OUT_4
- U3 pad 29: U3_TX-I2C2_SCL -> COM2_1
- U3 pad 30: U3_RX-I2C2_SDA -> COM2_2
- U3 pad 35: unconnected-(U3-PB14-Pad35) -> IO-0
- U3 pad 36: unconnected-(U3-PB15-Pad36) -> IO-1
- U3 pad 38: unconnected-(U3-PC7-Pad38) -> STAT_LED0
- U3 pad 39: unconnected-(U3-PC8-Pad39) -> STAT_LED1
- U3 pad 40: unconnected-(U3-PC9-Pad40) -> STAT_LED2
- U3 pad 41: unconnected-(U3-PA8-Pad41) -> HC_OUT_1
- U3 pad 42: unconnected-(U3-PA9-Pad42) -> HC_OUT_2
- U3 pad 43: unconnected-(U3-PA10-Pad43) -> IO-2
- U3 pad 46: unconnected-(U3-PA13-Pad46) -> SWDIO
- U3 pad 49: unconnected-(U3-PA14-Pad49) -> SWCLK
- U3 pad 50: unconnected-(U3-PA15-Pad50) -> SWO
- U3 pad 51: unconnected-(U3-PC10-Pad51) -> COM4_1
- U3 pad 52: unconnected-(U3-PC11-Pad52) -> COM4_2
- U3 pad 53: unconnected-(U3-PC12-Pad53) -> IO-3 (UART5 TX)
- U3 pad 54: unconnected-(U3-PD2-Pad54) -> IO-4 (UART5 RX)
- U3 pad 55: unconnected-(U3-PB3-Pad55) -> SPI1_SCK
- U3 pad 56: unconnected-(U3-PB4-Pad56) -> SPI1_MISO
- U3 pad 57: unconnected-(U3-PB5-Pad57) -> SPI1_MOSI
- U3 pad 58: unconnected-(U3-PB6-Pad58) -> COM2_1
- U3 pad 59: unconnected-(U3-PB7-Pad59) -> COM2_2
- U3 pad 61: unconnected-(U3-PB8-Pad61) -> SWITCH
- U3 pad 62: unconnected-(U3-PB9-Pad62) -> SPI_CS_FLASH
- U3 pad 8: unconnected-(U3-PC0-Pad8) -> I_sense_main
- U3 pad 9: unconnected-(U3-PC1-Pad9) -> vmain_sense
